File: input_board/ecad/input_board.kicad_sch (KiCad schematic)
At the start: 51 parts, among them J1 Conn_01x03_Male, J10 Conn_01x02_Female, J11 Conn_01x02_Female, J12 Conn_01x02_Female, J13 Conn_01x02_Female, J14 Conn_01x02_Female, J15 Conn_01x02_Female, J2 RCJ-041, J3 RCJ-041, J4 Conn_01x04_Female, J5 Conn_01x02_Female, J6 Conn_01x02_Female, J7 Conn_01x02_Female, J8 Conn_01x02_Female, J9 Conn_01x02_Female, Q1 BC817, Q2 IRFR5305, U1 NJM4580, U11 L7809, U6 MC33079

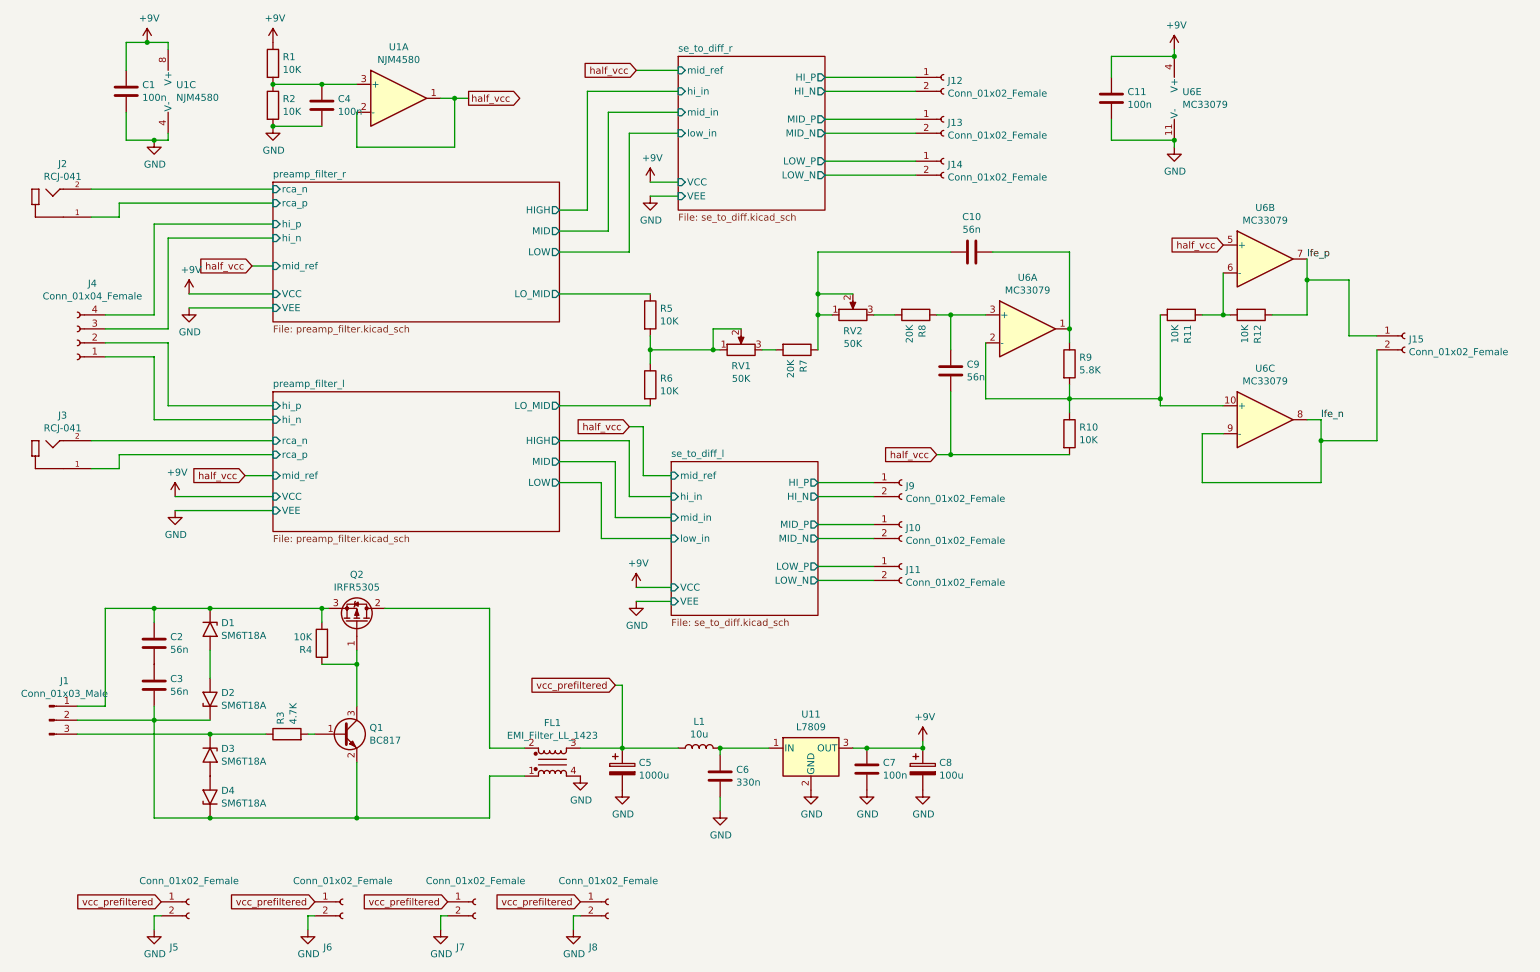
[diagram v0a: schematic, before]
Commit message: Input board: fix scematic and initial version of layout
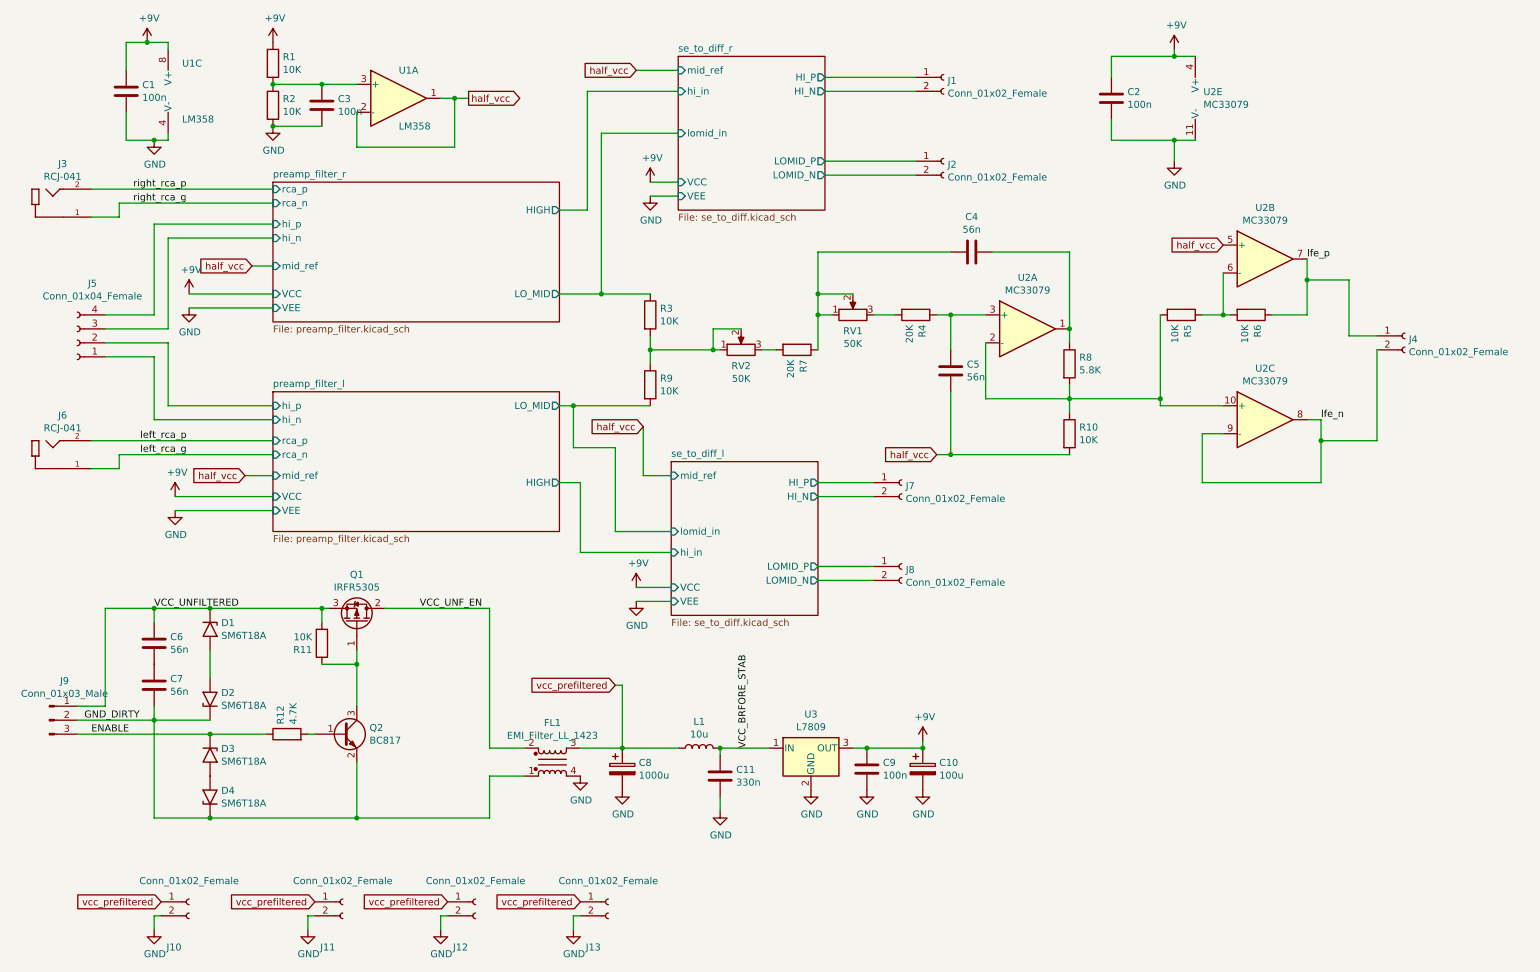
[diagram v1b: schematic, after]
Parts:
- removed J10, J13: Conn_01x02_Female, Connector_PinHeader_2.54mm:PinHeader_1x02_P2.54mm_Horizontal, symbol Connector:Conn_01x02_Female
- J10: renamed from J5; footprint Connector_Phoenix_MSTB:PhoenixContact_MSTBA_2,5_2-G_1x02_P5.00mm_Horizontal -> Connector_Phoenix_MC:PhoenixContact_MC_1,5_2-G-3.5_1x02_P3.50mm_Horizontal
- J11: renamed from J6; footprint Connector_Phoenix_MSTB:PhoenixContact_MSTBA_2,5_2-G_1x02_P5.00mm_Horizontal -> Connector_Phoenix_MC:PhoenixContact_MC_1,5_2-G-3.5_1x02_P3.50mm_Horizontal
- J12: renamed from J7; footprint Connector_Phoenix_MSTB:PhoenixContact_MSTBA_2,5_2-G_1x02_P5.00mm_Horizontal -> Connector_Phoenix_MC:PhoenixContact_MC_1,5_2-G-3.5_1x02_P3.50mm_Horizontal
- J13: renamed from J8; footprint Connector_Phoenix_MSTB:PhoenixContact_MSTBA_2,5_2-G_1x02_P5.00mm_Horizontal -> Connector_Phoenix_MC:PhoenixContact_MC_1,5_2-G-3.5_1x02_P3.50mm_Horizontal
- U1: value NJM4580 -> LM358; symbol Amplifier_Operational:NJM4580 -> Amplifier_Operational:LM358
- renumbered C8 to C10, C6 to C11, C11 to C2, C4 to C3, C10 to C4, C9 to C5, C2 to C6, C3 to C7, C5 to C8, C7 to C9, J12 to J1, J14 to J2, J2 to J3, J15 to J4, J4 to J5, J3 to J6, J9 to J7, J11 to J8, J1 to J9, Q2 to Q1, Q1 to Q2, R4 to R11, R3 to R12, R5 to R3, R8 to R4, R11 to R5, R12 to R6, R9 to R8, R6 to R9, RV2 to RV1, RV1 to RV2, U6 to U2, U11 to U3
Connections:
- net GND_DIRTY: now reaches C7.2, D2.1 (A1), D4.1 (A1), FL1.1, J9.2 (Pin_2), Q2.2 (E)
- net VCC_UNFILTERED: now reaches C6.1, D1.1 (A1), J9.1 (Pin_1), Q1.3 (S), R11.2
- net ENABLE: now reaches D3.1 (A1), J9.3 (Pin_3), R12.1
- net VCC_UNF_EN: now reaches FL1.2, Q1.2 (D)
- net VCC_BRFORE_STAB: now reaches C11.1, L1.2, U3.1 (IN)
- net preamp_filter_l/rca_n renamed left_rca_p
- net preamp_filter_l/rca_p renamed left_rca_g
- net preamp_filter_r/rca_n renamed right_rca_p
- net preamp_filter_r/rca_p renamed right_rca_g
- net se_to_diff_l/LOW_N renamed se_to_diff_l/LOMID_N
- net se_to_diff_l/LOW_P renamed se_to_diff_l/LOMID_P
- net se_to_diff_r/LOW_N renamed se_to_diff_r/LOMID_N
- net se_to_diff_r/LOW_P renamed se_to_diff_r/LOMID_P
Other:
- sheet preamp_filter_l ports: added none; removed LOW, MID
- sheet preamp_filter_r ports: added none; removed LOW, MID
- sheet se_to_diff_l ports: added LOMID_N, LOMID_P, lomid_in; removed LOW_N, LOW_P, MID_N, MID_P, low_in, mid_in
- sheet se_to_diff_r ports: added LOMID_N, LOMID_P, lomid_in; removed LOW_N, LOW_P, MID_N, MID_P, low_in, mid_in
- moved on the sheet: U2E
